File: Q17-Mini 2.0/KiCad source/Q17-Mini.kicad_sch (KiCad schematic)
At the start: 83 parts, among them J1 INPUT, J2-1 SPK+, J2-2 SPK-, J3-1 V+, J3-2 GND, J3-3 V-, Q1 IRF610, Q10 KSA992, Q12 KSC1845, Q13 IRF610, Q14 IRF9610, Q15 FQA46N15, Q16 IXTH48P20P, Q2 KSA992, Q3 KSC1845, Q4 IRF9610, Q5 FQPF7P20, Q6 2SK3564, Q7 LSK170B, Q8 DN2540, Q9 BS250P, U1 OPA1611, U2 NDC7003P

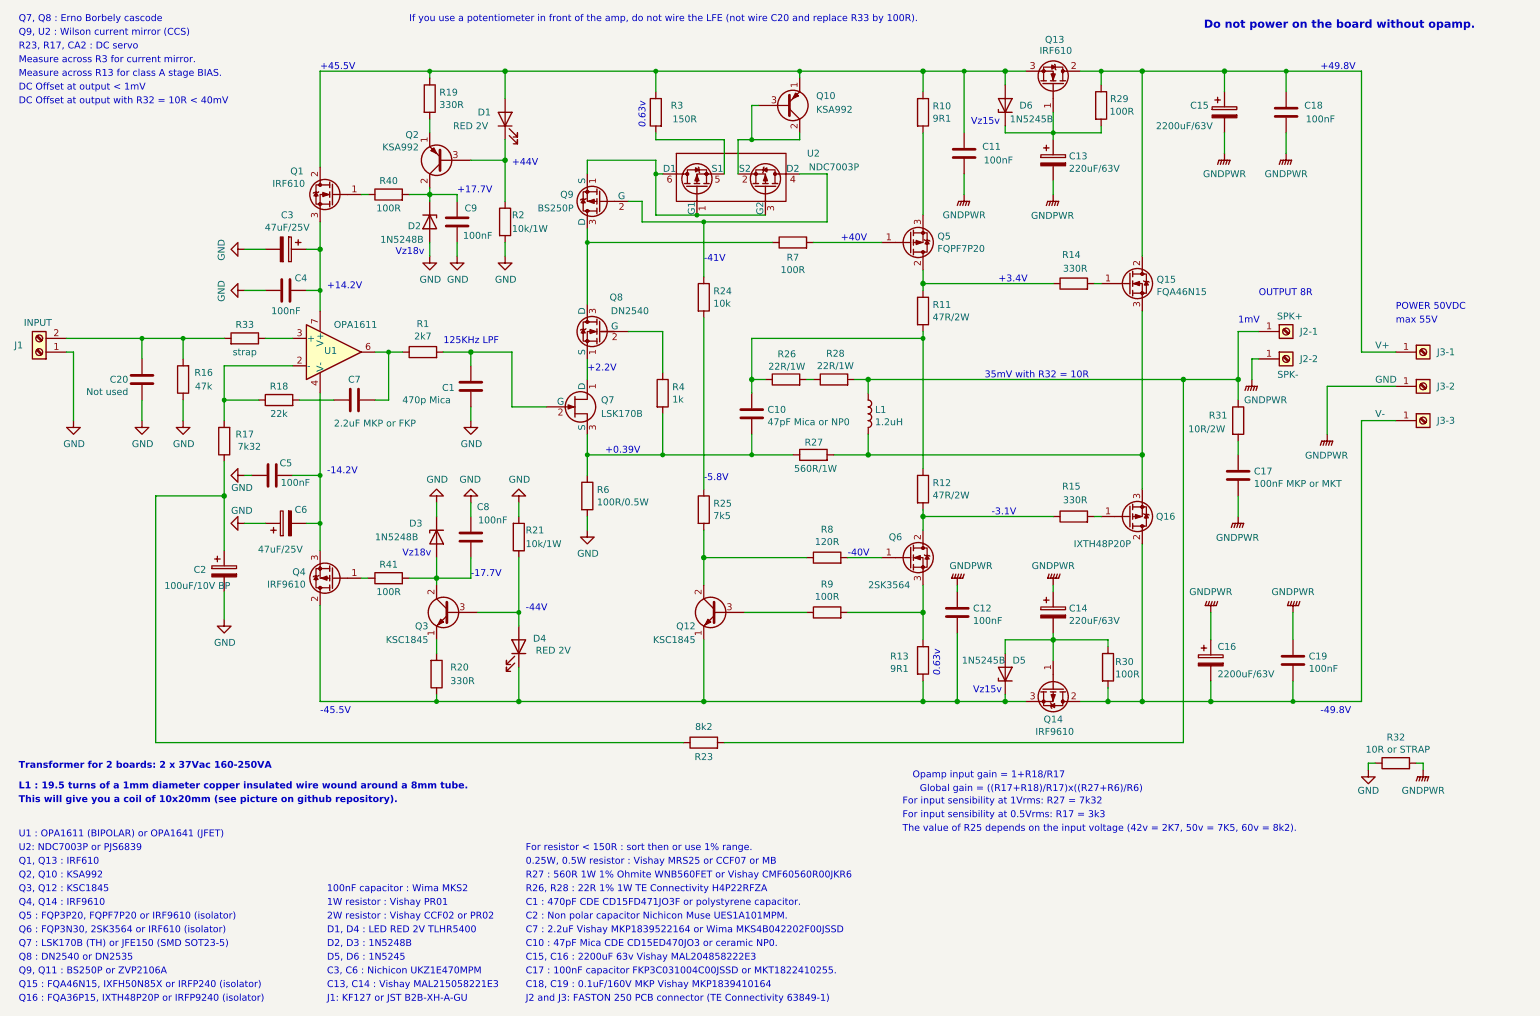
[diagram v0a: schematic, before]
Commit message: Update Q17-Mini diagram and measures
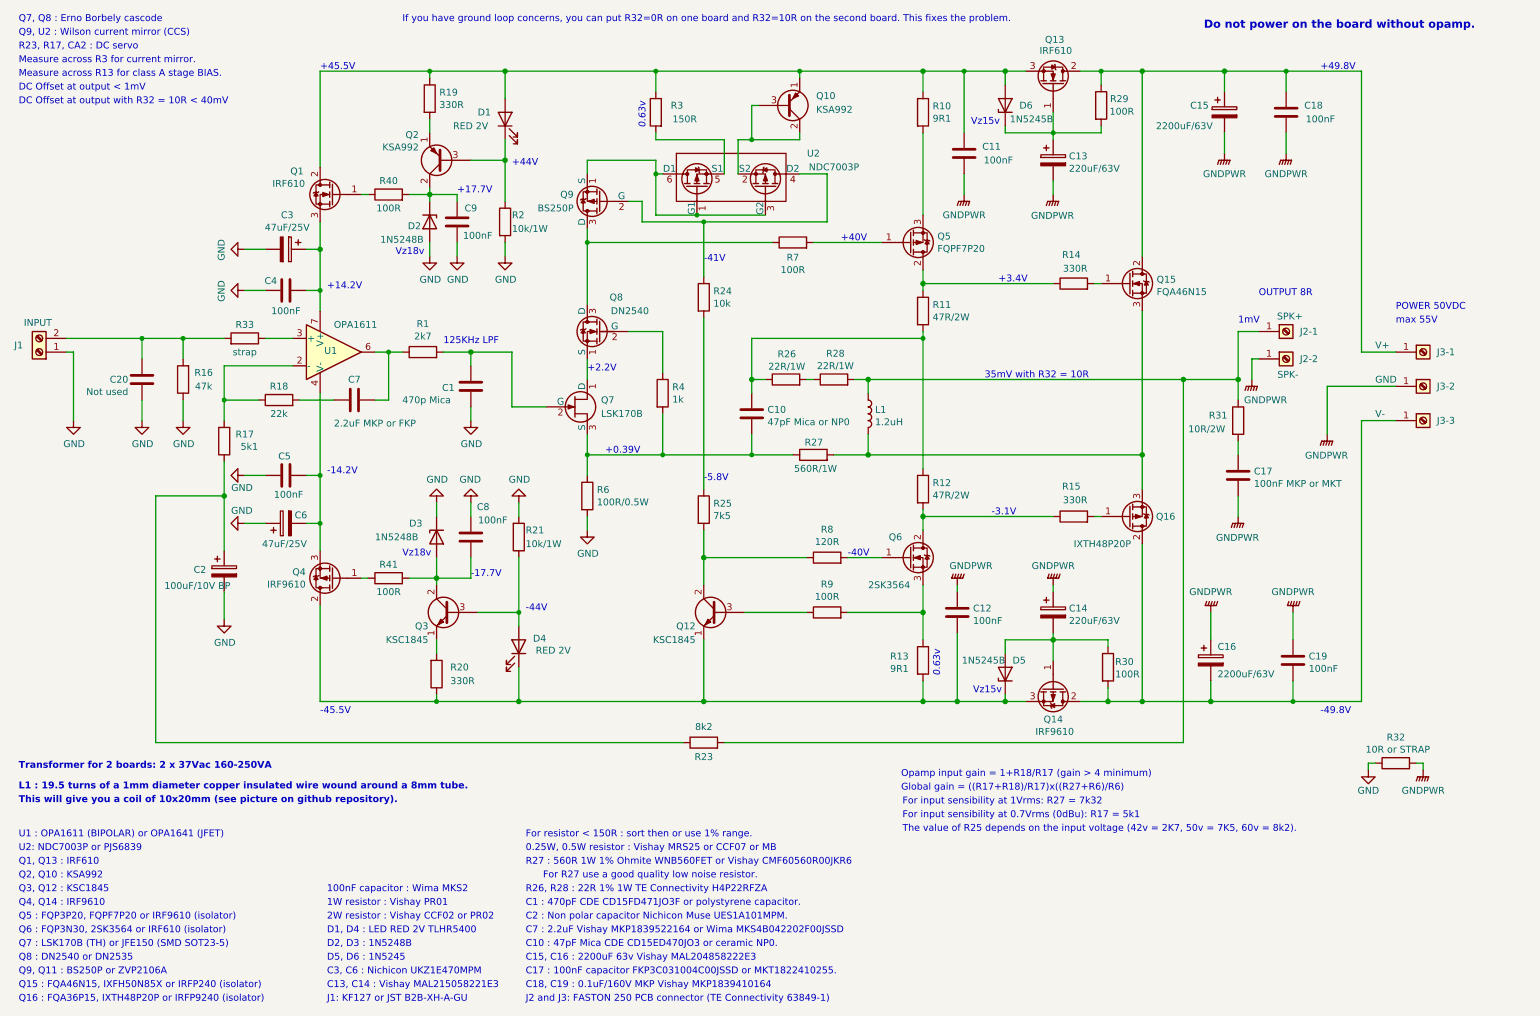
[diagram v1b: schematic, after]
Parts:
- R17: value 7k32 -> 5k1; Mouser 594-MRS25000C4991FRP -> 594-MRS25000C5101FRP; Part# MRS25000C4991FRP00 -> MRS25000C5101FRP00
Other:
- note added: "For R27 use a good quality low noise resistor."
- note added: "For input sensibility at 0.7Vrms (0dBu): R17 = 5k1"
- note added: "If you have ground loop concerns, you can put R32=0R on one board and R32=10R on the second board. This fixes the problem."
- note added: "Opamp input gain = 1+R18/R17 (gain > 4 minimum)"
- note removed: "For input sensibility at 0.5Vrms: R17 = 3k3"
- note removed: "If you use a potentiometer in front of the amp, do not wire the LFE (not wire C20 and replace R33 by 100R)."
- note removed: "Opamp input gain = 1+R18/R17"
- moved on the sheet: C5
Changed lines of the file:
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@@
 	(title_block
 		(title "Q17-Mini Amplifier 2.x")
-		(date "2024-05-21")
-		(rev "2.0.7")
+		(date "2024-05-27")
+		(rev "2.0.8")
 		(company "by eng. Tiberiu Vicol")
 		(comment 1 "Modified by Stef for the Q17-Mini project")
@@
 	(wire
 		(pts
-			(xy 64.77 99.06) (xy 69.85 99.06)
+			(xy 67.31 99.06) (xy 69.85 99.06)
 		)
 		(stroke
@@
 	(wire
 		(pts
-			(xy 55.88 99.06) (xy 57.15 99.06)
+			(xy 55.88 99.06) (xy 59.69 99.06)
 		)
 		(stroke
@@
 		)
 	)
-	(text "Opamp input gain = 1+R18/R17"
+	(text "Opamp input gain = 1+R18/R17 (gain > 4 minimum)"
 		(exclude_from_sim no)
-		(at 193.802 154.686 0)
+		(at 177.546 154.432 0)
 		(effects
 			(font
 				(size 1.27 1.27)
 			)
+			(justify left)
 		)
 	)
@@
 		)
 	)
+	(text "If you have ground loop concerns, you can put R32=0R on one board and R32=10R on the second board. This fixes the problem."
+		(exclude_from_sim no)
+		(at 85.09 15.24 0)
+		(effects
+			(font
+				(size 1.27 1.27)
+			)
+			(justify left bottom)
+		)
+	)
 	(text "+3.4V"
 		(exclude_from_sim no)
@@
 	(text "For resistor < 150R : sort then or use 1% range."
 		(exclude_from_sim no)
-		(at 107.95 168.91 0)
+		(at 107.95 166.37 0)
 		(effects
 			(font
@@
 		)
 	)
+	(text "For R27 use a good quality low noise resistor."
+		(exclude_from_sim no)
+		(at 131.064 173.228 0)
+		(effects
+			(font
+				(size 1.27 1.27)
+			)
+		)
+	)
 	(text "Measure across R13 for class A stage BIAS."
 		(exclude_from_sim no)
@@
 		)
 	)
-	(text "For input sensibility at 0.5Vrms: R17 = 3k3"
+	(text "For input sensibility at 0.7Vrms (0dBu): R17 = 5k1"
 		(exclude_from_sim no)
 		(at 177.8 162.814 0)
@@
 	(text "Global gain = ((R17+R18)/R17)x((R27+R6)/R6)"
 		(exclude_from_sim no)
-		(at 201.676 157.226 0)
+		(at 177.546 156.972 0)
 		(effects
 			(font
 				(size 1.27 1.27)
 			)
+			(justify left)
 		)
 	)
 	(text "0.25W, 0.5W resistor : Vishay MRS25 or CCF07 or MB"
 		(exclude_from_sim no)
-		(at 107.95 171.45 0)
+		(at 107.95 168.91 0)
 		(effects
 			(font
@@
 	(text "R27 : 560R 1W 1% Ohmite WNB560FET or Vishay CMF60560R00JKR6"
 		(exclude_from_sim no)
-		(at 107.95 173.99 0)
+		(at 107.95 171.45 0)
 		(effects
 			(font
@@
 		)
 	)
-	(text "If you use a potentiometer in front of the amp, do not wire the LFE (not wire C20 and replace R33 by 100R)."
-		(exclude_from_sim no)
-		(at 86.36 15.24 0)
-		(effects
-			(font
-				(size 1.27 1.27)
-			)
-			(justify left bottom)
-		)
-	)
 	(text "Do not power on the board without opamp."
 		(exclude_from_sim no)
@@
 	(symbol
 		(lib_id "Device:C")
-		(at 60.96 99.06 90)
+		(at 63.5 99.06 90)
 		(unit 1)
 		(exclude_from_sim no)
@@
 		(dnp no)
 		(property "Reference" "C5"
-			(at 63.5 96.774 90)
+			(at 63.246 95.504 90)
 			(effects
 				(font
@@
 		)
 		(property "Value" "100nF"
-			(at 65.2658 100.4056 90)
+			(at 64.008 102.616 90)
 			(effects
 				(font
@@
 		)
 		(property "Footprint" "Capacitor_THT:C_Rect_L7.2mm_W2.5mm_P5.00mm_FKS2_FKP2_MKS2_MKP2"
-			(at 64.77 98.0948 0)
+			(at 67.31 98.0948 0)
 			(effects
 				(font
@@
 		)
 		(property "Datasheet" "https://www.mouser.fr/datasheet/2/440/e_WIMA_MKS_2-1139871.pdf"
-			(at 60.96 99.06 0)
+			(at 63.5 99.06 0)
 			(effects
 				(font
@@
 		)
 		(property "Description" ""
-			(at 60.96 99.06 0)
+			(at 63.5 99.06 0)
 			(effects
 				(font
@@
 		)
 		(property "Part#" "MKS2D031001A00KSSD"
-			(at 60.96 99.06 90)
+			(at 63.5 99.06 90)
 			(effects
 				(font
@@
 		)
 		(property "Mouser" "505-MKS2.1/100/10"
-			(at 60.96 99.06 90)
+			(at 63.5 99.06 90)
 			(effects
 				(font
@@
 		(dnp no)
 		(property "Reference" "C6"
-			(at 66.294 105.41 90)
+			(at 66.294 106.426 90)
 			(effects
 				(font
@@
 		)
 		(property "Value" "47uF/25V"
-			(at 62.484 112.776 90)
+			(at 63.246 111.76 90)
 			(effects
 				(font
@@
 			)
 		)
-		(property "Value" "7k32"
+		(property "Value" "5k1"
 			(at 56.7302 93.7195 0)
 			(effects
@@
 			)
 		)
-		(property "Description" "4k99 resistor"
+		(property "Description" "5k1 resistor"
 			(at 52.07 92.71 0)
 			(effects
@@
 			)
 		)
-		(property "Part#" "MRS25000C4991FRP00"
+		(property "Part#" "MRS25000C5101FRP00"
 			(at 52.07 92.71 0)
 			(effects
@@
 			)
 		)
-		(property "Mouser" "594-MRS25000C4991FRP"
+		(property "Mouser" "594-MRS25000C5101FRP"
 			(at 52.07 92.71 0)
 			(effects
@@
 		(dnp no)
 		(property "Reference" "C4"
-			(at 66.294 62.484 90)
+			(at 60.706 62.992 90)
 			(effects
 				(font

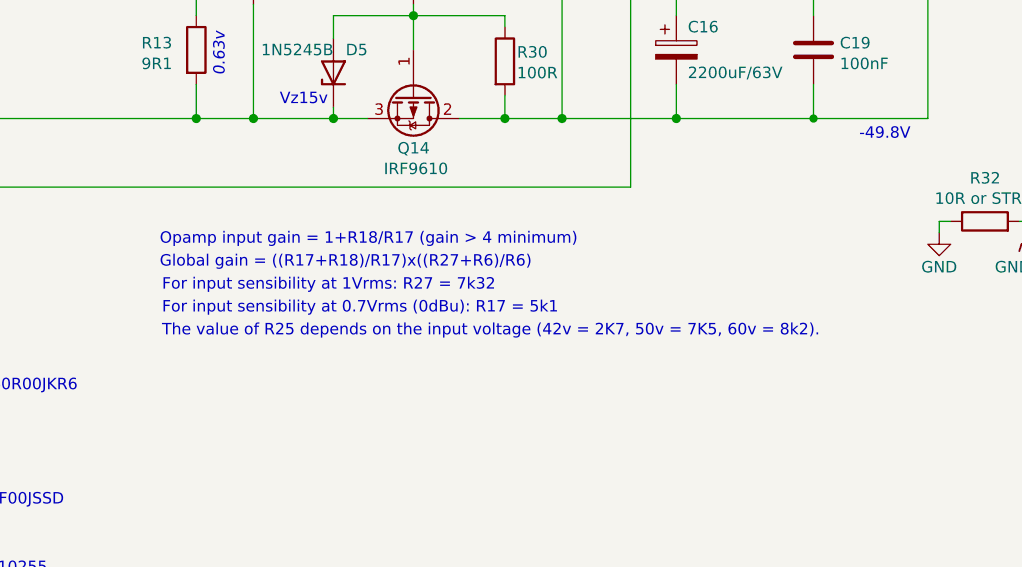
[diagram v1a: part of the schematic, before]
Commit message: Update Q17-Mini diagram
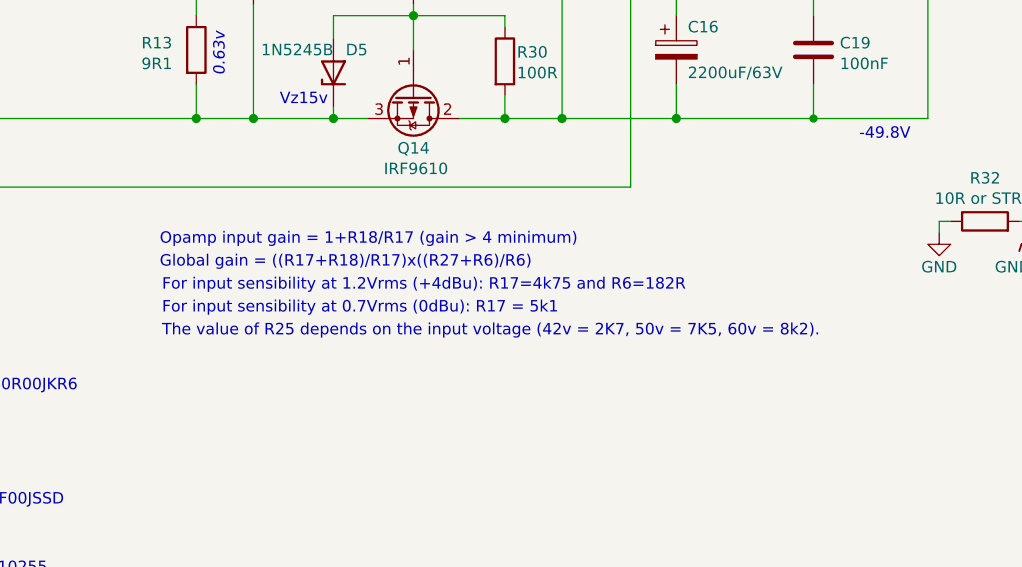
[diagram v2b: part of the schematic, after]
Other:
- note added: "For input sensibility at 1.2Vrms (+4dBu): R17=4k75 and R6=182R"
- note removed: "For input sensibility at 1Vrms: R27 = 7k32"
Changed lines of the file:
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@@
 	(title_block
 		(title "Q17-Mini Amplifier 2.x")
-		(date "2024-05-27")
-		(rev "2.0.8")
+		(date "2024-05-28")
+		(rev "2.0.9")
 		(company "by eng. Tiberiu Vicol")
 		(comment 1 "Modified by Stef for the Q17-Mini project")
@@
 		)
 	)
-	(text "For input sensibility at 1Vrms: R27 = 7k32"
+	(text "For input sensibility at 1.2Vrms (+4dBu): R17=4k75 and R6=182R"
 		(exclude_from_sim no)
 		(at 177.8 160.274 0)
